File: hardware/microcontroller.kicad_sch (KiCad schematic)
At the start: 53 parts, among them J501 PRPC006SAAN-RC, J502 TC2050, J503 61300611121, J504 61300611121, J505 61300611121, J506 61300611121, J507 61300611121, J508 PRPC001DAAN-RC, J509 PRPC006SAAN-RC, Q501 BSS806NH, U501 STM32L552CEU6, U502 AT25SF081B-MAHB-T, Y501 ECS-160-9-37-CKM-TR3, Y502 ABS05-32.768KHZ-9-T

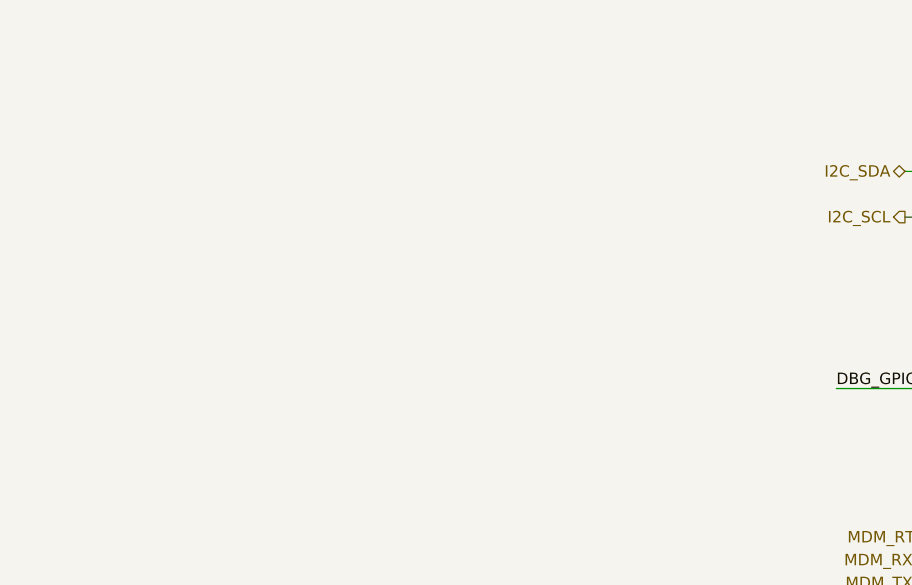
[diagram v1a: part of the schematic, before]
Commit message: HW: Add optional user button to PA9
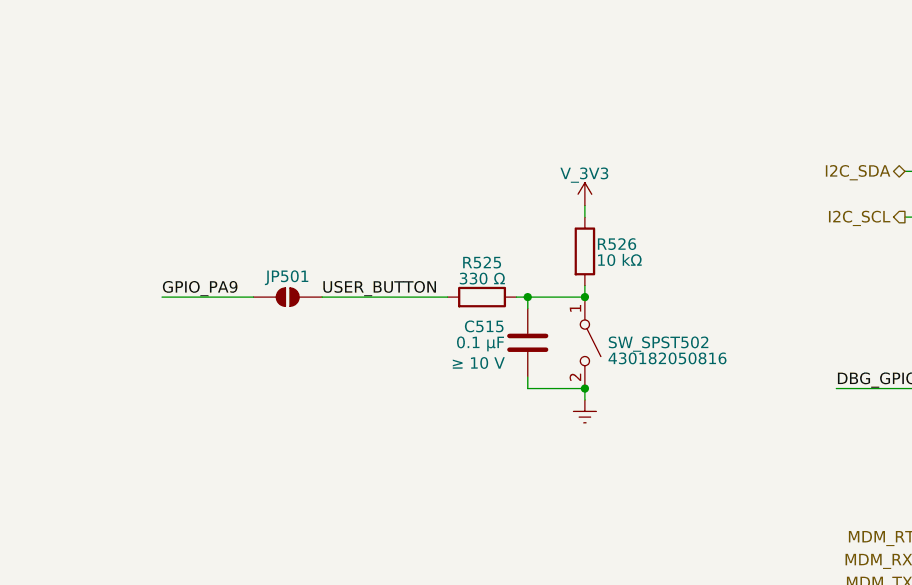
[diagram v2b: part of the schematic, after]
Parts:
- added C515: 0.1 µF, perfect_footprints:C_0402_1005Metric, symbol Device:C
- added JP501: SolderJumper_2_Open, Jumper:SolderJumper-2_P1.3mm_Open_TrianglePad1.0x1.5mm, symbol Jumper:SolderJumper_2_Open
- added R525: 330 Ω, perfect_footprints:R_0402_1005Metric, symbol Device:R
- added R526: 10 kΩ, perfect_footprints:R_0402_1005Metric, symbol Device:R
- added SW_SPST502: 430182050816, Button_Switch_SMD:SW_SPST_PTS645, symbol Switch:SW_SPST
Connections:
- net GND: now also C515.2, SW_SPST502.2 (B)
- net GPIO_PA9: now also JP501.1 (A)
- net V_3V3: now also R526.1
- new net: C515.1, R525.1, R526.2, SW_SPST502.1 (A)
- new net USER_BUTTON: JP501.2 (B), R525.2

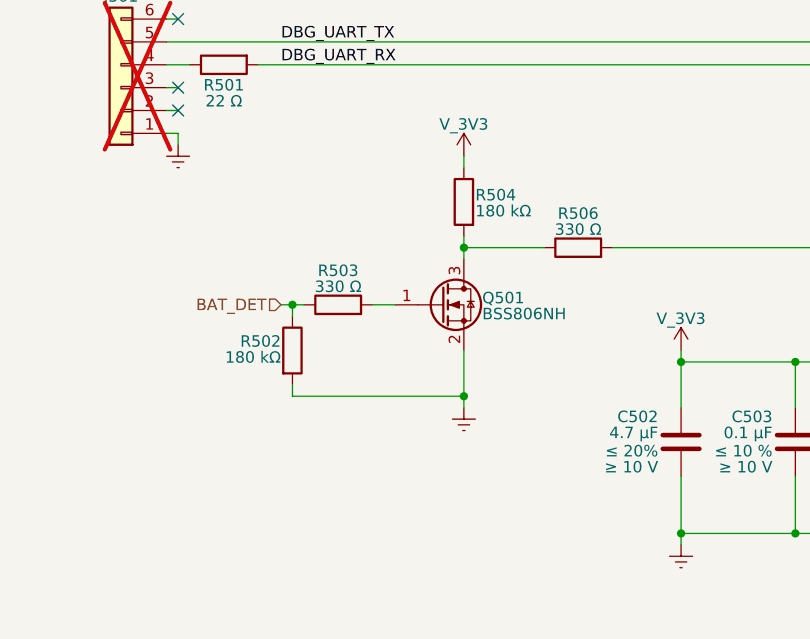
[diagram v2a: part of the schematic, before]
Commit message: HW: Fix errors found in testing
- Add more test points for Modem facing UART
- Fix buck-boost feedback resistors
- DNP the battery detection circuit
- Switch Modem UART voltage translator to UQFN
  - Add 0 Ohm resistors for the direction choices
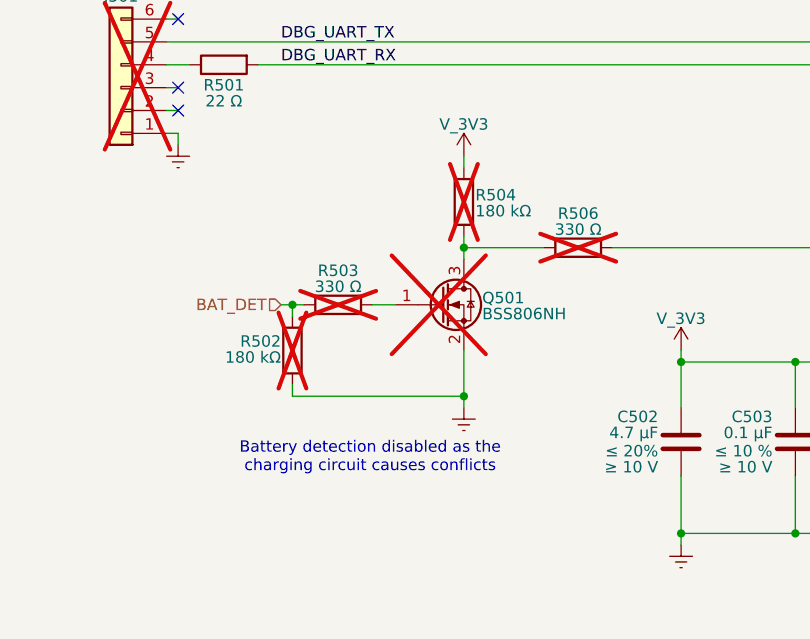
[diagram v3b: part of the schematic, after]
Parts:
- Q501, R502, R503, R504, R506: now not fitted; now left out of the parts list
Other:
- note added: "Battery detection disabled as the charging circuit causes conflicts"
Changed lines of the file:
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@@
 	(title_block
 		(title "Iida devkit")
-		(date "2025-06-13")
-		(rev "v5.0.0")
+		(date "2025-07-30")
+		(rev "v5.1.0")
 	)
 	(text "Reset switch"
@@
 		)
 	)
+	(text "Battery detection disabled as the\ncharging circuit causes conflicts"
+		(exclude_from_sim no)
+		(at 103.886 193.04 0)
+		(effects
+			(font
+				(size 1.27 1.27)
+			)
+			(justify top)
+		)
+	)
 	(text "Place the GPIO headers along the edges of the PCB."
 		(exclude_from_sim no)
@@
 		(unit 1)
 		(exclude_from_sim no)
-		(in_bom yes)
+		(in_bom no)
 		(on_board yes)
-		(dnp no)
+		(dnp yes)
 		(property "Reference" "R504"
 			(at 115.57 165.608 0)
@@
 		(unit 1)
 		(exclude_from_sim no)
-		(in_bom yes)
+		(in_bom no)
 		(on_board yes)
-		(dnp no)
+		(dnp yes)
 		(property "Reference" "R506"
 			(at 127 168.402 90)
@@
 		(unit 1)
 		(exclude_from_sim no)
-		(in_bom yes)
+		(in_bom no)
 		(on_board yes)
-		(dnp no)
+		(dnp yes)
 		(property "Reference" "R503"
 			(at 100.33 174.752 90)
@@
 		(unit 1)
 		(exclude_from_sim no)
-		(in_bom yes)
+		(in_bom no)
 		(on_board yes)
-		(dnp no)
+		(dnp yes)
 		(property "Reference" "R502"
 			(at 93.98 181.864 0)
@@
 		(unit 1)
 		(exclude_from_sim no)
-		(in_bom yes)
+		(in_bom no)
 		(on_board yes)
-		(dnp no)
+		(dnp yes)
 		(property "Reference" "Q501"
 			(at 116.332 177.038 0)

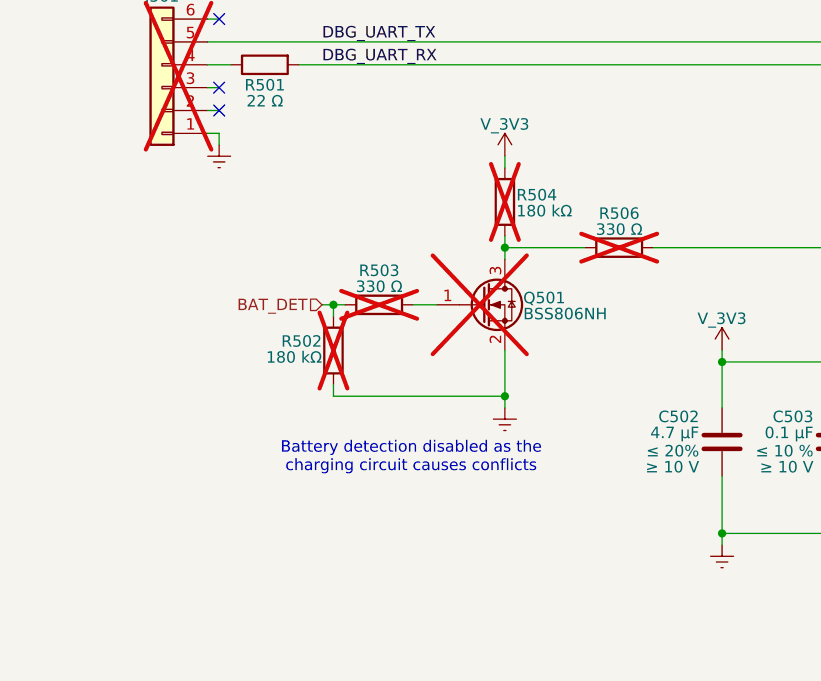
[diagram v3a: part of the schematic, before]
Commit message: HW: Use Power OR ST pin for BAT_DET
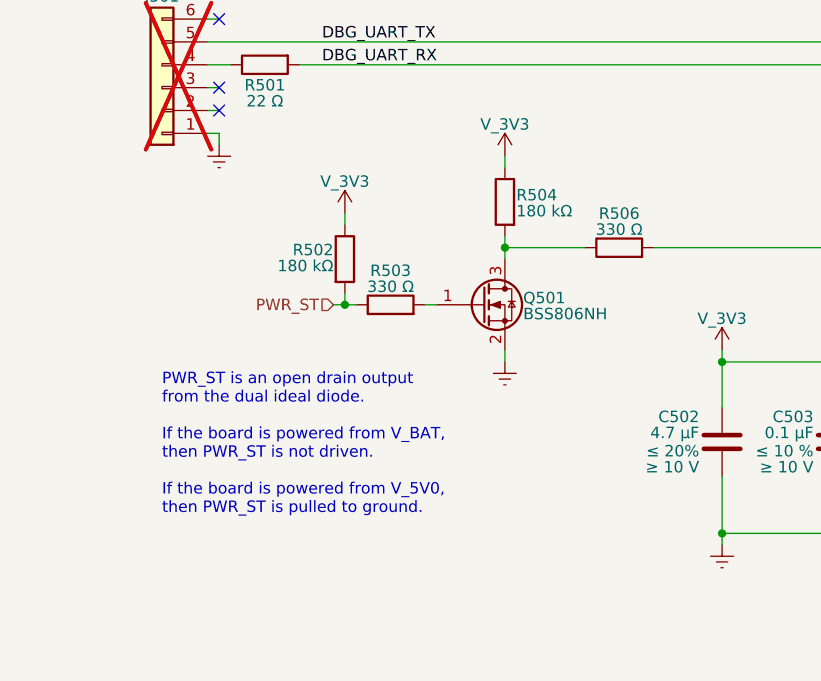
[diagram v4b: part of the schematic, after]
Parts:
- Q501, R502, R503, R504, R506: now fitted; now in the parts list
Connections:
- net GND: no longer R502.2
- net V_3V3: now also R502.1
- net BAT_DET renamed PWR_ST
- net PWR_ST: now also R502.2; no longer R502.1
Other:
- note added: "PWR_ST is an open drain output from the dual ideal diode. If the board is powered from V_BAT, then PWR_ST is not driven. If the board is powered from V_5V0, then PWR_ST is pulled to ground."
- note removed: "Battery detection disabled as the charging circuit causes conflicts"

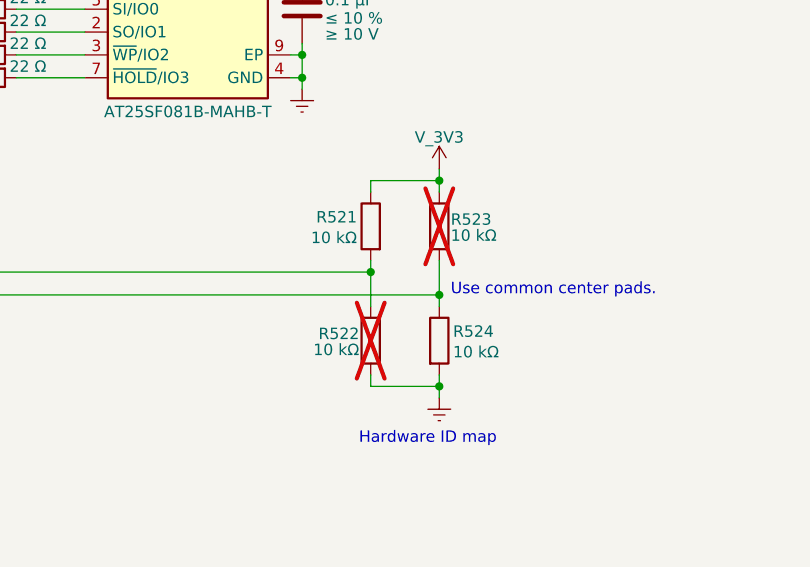
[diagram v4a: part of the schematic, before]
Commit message: HW: Fix BOM and add v5.1.0 to HWID map
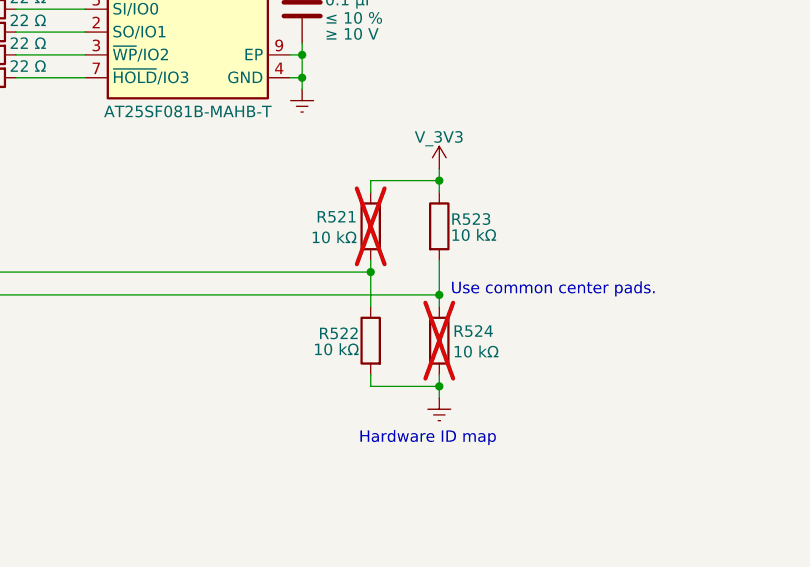
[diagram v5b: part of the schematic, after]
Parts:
- R508: now left out of the parts list
- R521, R524: now not fitted; now left out of the parts list
- R522, R523: now fitted
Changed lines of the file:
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@@
 				)
 			)
-			(table_cell "TBD"
+			(table_cell "v5.1.0"
 				(exclude_from_sim no)
 				(at 321.31 161.29 0)
@@
 		(in_bom yes)
 		(on_board yes)
-		(dnp yes)
+		(dnp no)
 		(property "Reference" "R523"
 			(at 318.77 127.508 0)
@@
 		(unit 1)
 		(exclude_from_sim no)
-		(in_bom yes)
+		(in_bom no)
 		(on_board yes)
 		(dnp yes)
@@
 		(unit 1)
 		(exclude_from_sim no)
-		(in_bom yes)
+		(in_bom no)
 		(on_board yes)
-		(dnp no)
+		(dnp yes)
 		(property "Reference" "R524"
 			(at 319.024 139.954 0)
@@
 		(unit 1)
 		(exclude_from_sim no)
-		(in_bom yes)
+		(in_bom no)
 		(on_board yes)
-		(dnp no)
+		(dnp yes)
 		(property "Reference" "R521"
 			(at 308.356 127.254 0)
@@
 		(in_bom yes)
 		(on_board yes)
-		(dnp yes)
+		(dnp no)
 		(property "Reference" "R522"
 			(at 308.61 140.208 0)

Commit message: HW: Update BOM
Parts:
- renumbered SW_SPST501 to SW501, SW_SPST502 to SW502
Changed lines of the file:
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@@
 	(title_block
 		(title "Iida devkit")
-		(date "2025-07-31")
+		(date "2025-09-02")
 		(rev "v5.1.0")
 	)
@@
 		(on_board yes)
 		(dnp no)
-		(property "Reference" "SW_SPST501"
+		(property "Reference" "SW501"
 			(at 116.84 132.08 90)
 			(effects
@@
 			(project "iida_devkit"
 				(path "/b12a6e25-97fb-4aba-bc96-af8db389bb9a/6dd8d741-3080-458c-a4f5-a05a3905bb8a"
-					(reference "SW_SPST501")
+					(reference "SW501")
 					(unit 1)
 				)
@@
 		(on_board yes)
 		(dnp no)
-		(property "Reference" "SW_SPST502"
+		(property "Reference" "SW502"
 			(at 358.14 195.58 90)
 			(effects
@@
 			(project "iida_devkit"
 				(path "/b12a6e25-97fb-4aba-bc96-af8db389bb9a/6dd8d741-3080-458c-a4f5-a05a3905bb8a"
-					(reference "SW_SPST502")
+					(reference "SW502")
 					(unit 1)
 				)

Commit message: HW: Start fixing found issues
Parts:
- J501, J509: DigiKey Part Number (none) -> 732-5319-ND; MPN PRPC006SAAN-RC -> 61300611121; Manufacturer Sullins Connector Solutions -> Würth Elektronik
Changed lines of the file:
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@@
 		(title "Iida devkit")
 		(date "2025-09-02")
-		(rev "v5.1.0")
+		(rev "v5.1.1")
 	)
 	(text "Reset switch"
@@
 			)
 		)
-		(property "Manufacturer" "Sullins Connector Solutions"
+		(property "Manufacturer" "Würth Elektronik"
 			(at 76.2 153.67 0)
 			(effects
@@
 			)
 		)
-		(property "MPN" "PRPC006SAAN-RC"
+		(property "MPN" "61300611121"
 			(at 76.2 153.67 0)
 			(effects
@@
 			)
 		)
+		(property "DigiKey Part Number" "732-5319-ND"
+			(at 76.2 153.67 0)
+			(effects
+				(font
+					(size 1.27 1.27)
+				)
+				(hide yes)
+			)
+		)
 		(pin "3"
 		)
@@
 			)
 		)
-		(property "Manufacturer" "Sullins Connector Solutions"
+		(property "Manufacturer" "Würth Elektronik"
 			(at 402.59 224.79 0)
 			(effects
@@
 			)
 		)
-		(property "MPN" "PRPC006SAAN-RC"
+		(property "MPN" "61300611121"
 			(at 402.59 224.79 0)
 			(effects
@@
 			(at 402.59 224.79 0)
 			(effects
+				(font
+					(size 1.27 1.27)
+				)
+				(hide yes)
+			)
+		)
+		(property "DigiKey Part Number" "732-5319-ND"
+			(at 402.59 224.79 0)
+			(effects

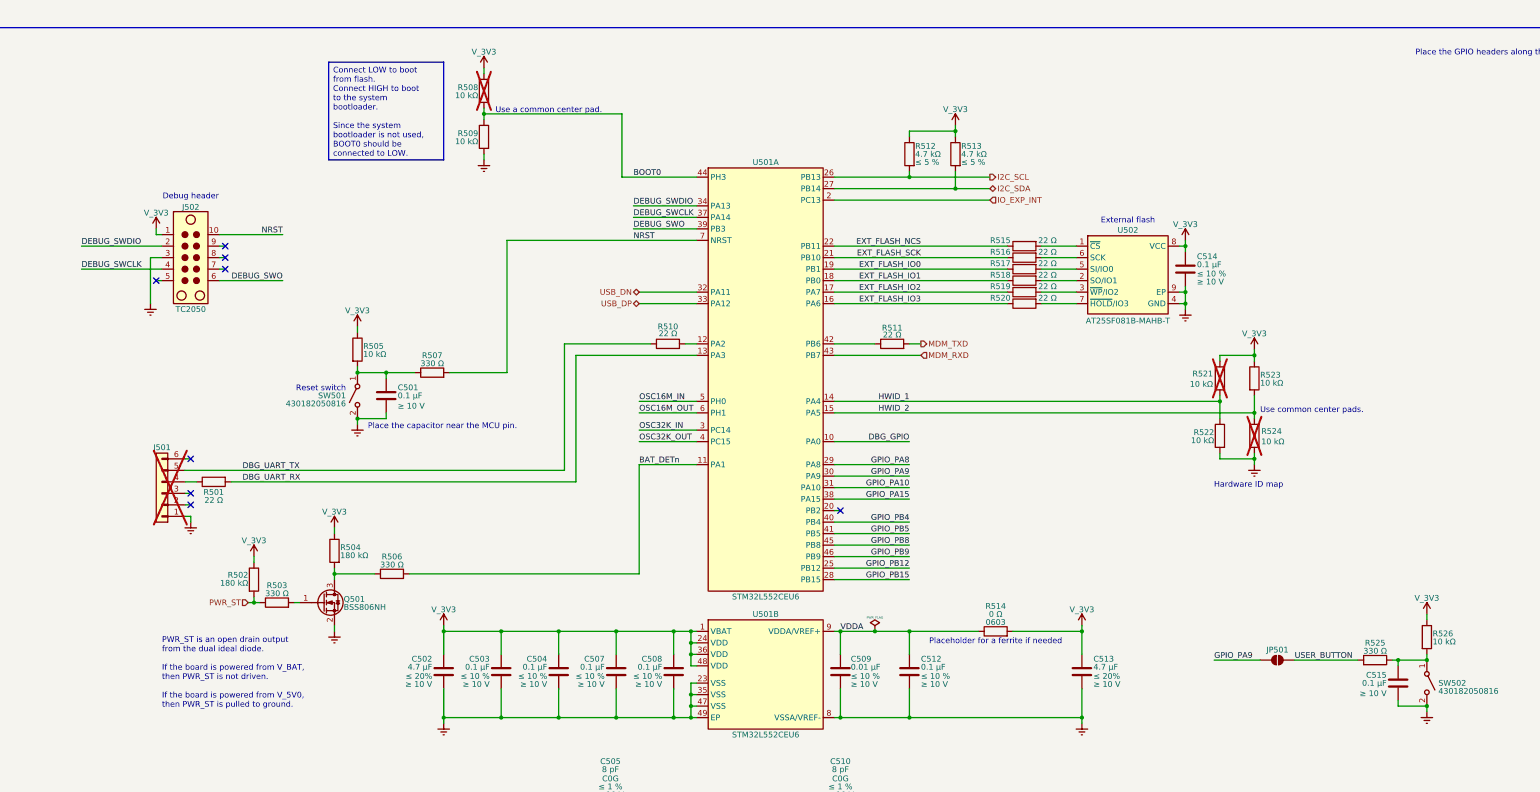
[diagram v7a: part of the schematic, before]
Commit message: HW: Fix battery detection
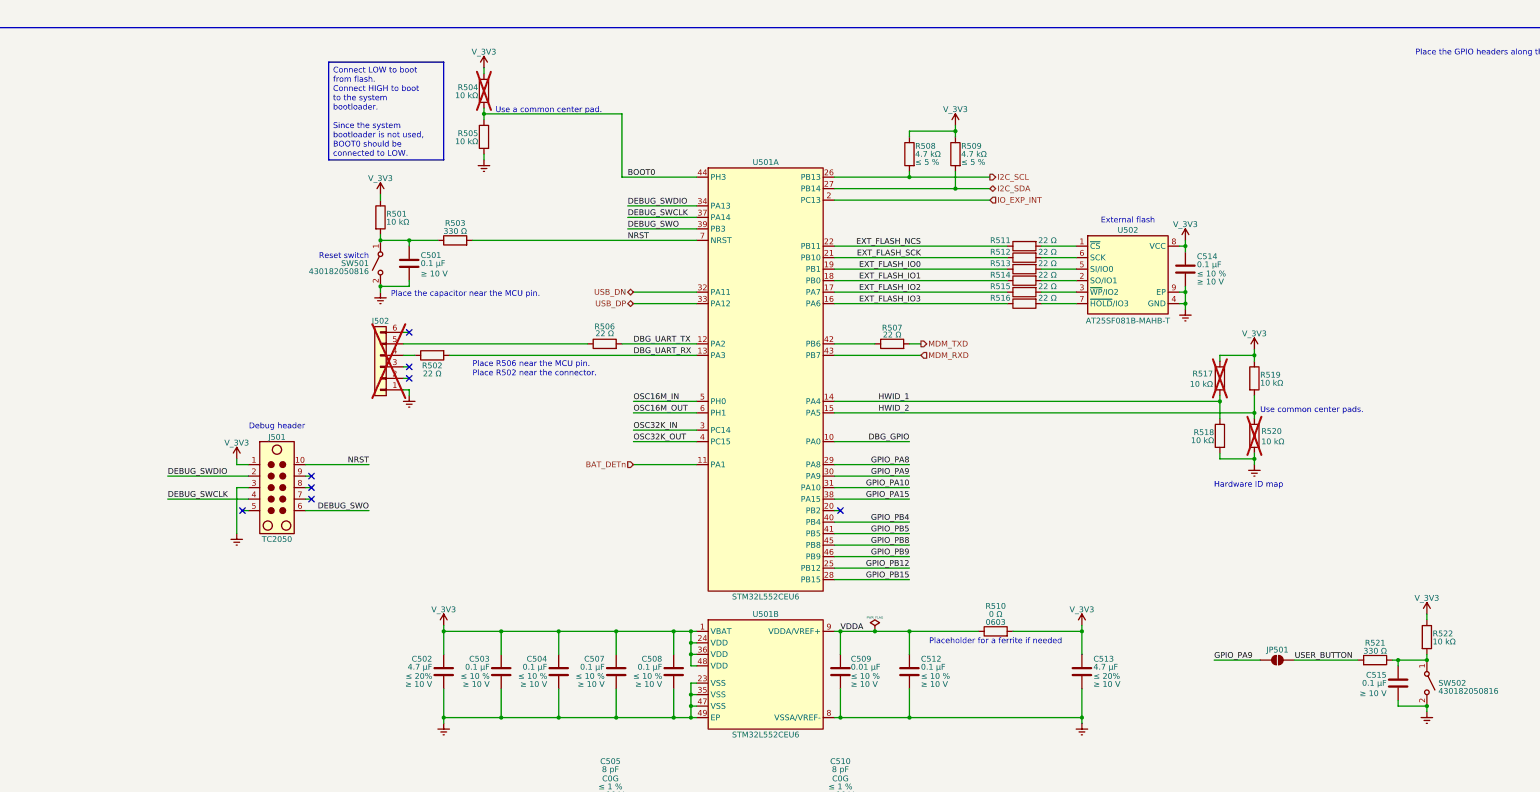
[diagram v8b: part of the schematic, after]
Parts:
- removed Q501: BSS806NH, Package_TO_SOT_SMD:SOT-23-3, symbol Transistor_FET:Q_NMOS_GSD
- removed R502, R504: 180 kΩ, perfect_footprints:R_0402_1005Metric, symbol Device:R
- removed R503, R506: 330 Ω, perfect_footprints:R_0402_1005Metric, symbol Device:R
- renumbered J502 to J501, J501 to J502, R505 to R501, R501 to R502, R507 to R503, R508 to R504, R509 to R505, R510 to R506, R511 to R507, R512 to R508, R513 to R509, R514 to R510, R515 to R511, R516 to R512, R517 to R513, R518 to R514, R519 to R515, R520 to R516, R521 to R517, R522 to R518, R523 to R519, R524 to R520, R525 to R521, R526 to R522
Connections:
- net DBG_UART_TX: now also R506.2, U501.12 (PA2); no longer J502.5 (Pin_5), R506.1
- new net: J502.5 (Pin_5), R506.1
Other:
- note added: "Place R506 near the MCU pin. Place R502 near the connector."
- note removed: "PWR_ST is an open drain output from the dual ideal diode. If the board is powered from V_BAT, then PWR_ST is not driven. If the board is powered from V_5V0, then PWR_ST is pulled to ground."
- moved on the sheet: C501, J501, J502, R501, R502, R503, R506, SW501
